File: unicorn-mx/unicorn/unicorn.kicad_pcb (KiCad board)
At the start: 2 copper layers, 267.6 x 110.5 mm, 118 parts, among them J2 USB_C, K1 KEYSW, K10 KEYSW, K11 KEYSW, K12 KEYSW, K13 KEYSW, K14 KEYSW, K15 KEYSW, K16 KEYSW, K17 KEYSW, K18 KEYSW, K19 KEYSW, K2 KEYSW, K20 KEYSW, K21 KEYSW, K22 KEYSW, K23 KEYSW, K24 KEYSW, K25 KEYSW, K26 KEYSW, K27 KEYSW, K28 KEYSW, K29 KEYSW, K3 KEYSW, K30 KEYSW, K31 KEYSW, K32 KEYSW, K33 KEYSW, K34 KEYSW, K35 KEYSW, K36 KEYSW, K37 KEYSW, K38 KEYSW, K39 KEYSW, K4 KEYSW, K40 KEYSW, K41 KEYSW, K42 KEYSW, K43 KEYSW, K44 KEYSW, K5 KEYSW, K6 KEYSW, K7 KEYSW, K8 KEYSW, K9 KEYSW, Q1 MMBT3904, SW1 SW_Push, SW2 Rotary_Encoder_Switch, SW3 Rotary_Encoder_Switch, U1 XC6206PxxxMR, U3 STM32F072CBUx, U4 SRV05-4

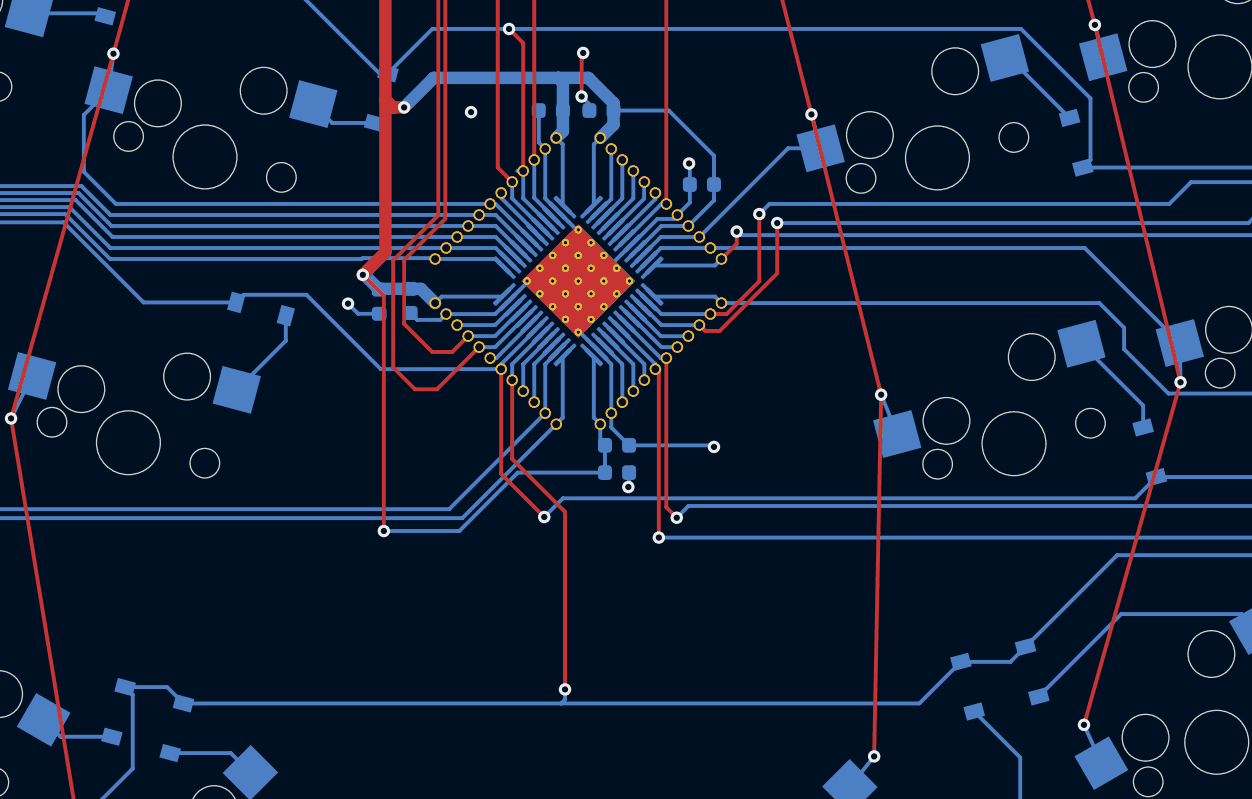
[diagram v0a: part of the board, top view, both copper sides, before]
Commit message: add 3d models, add oled
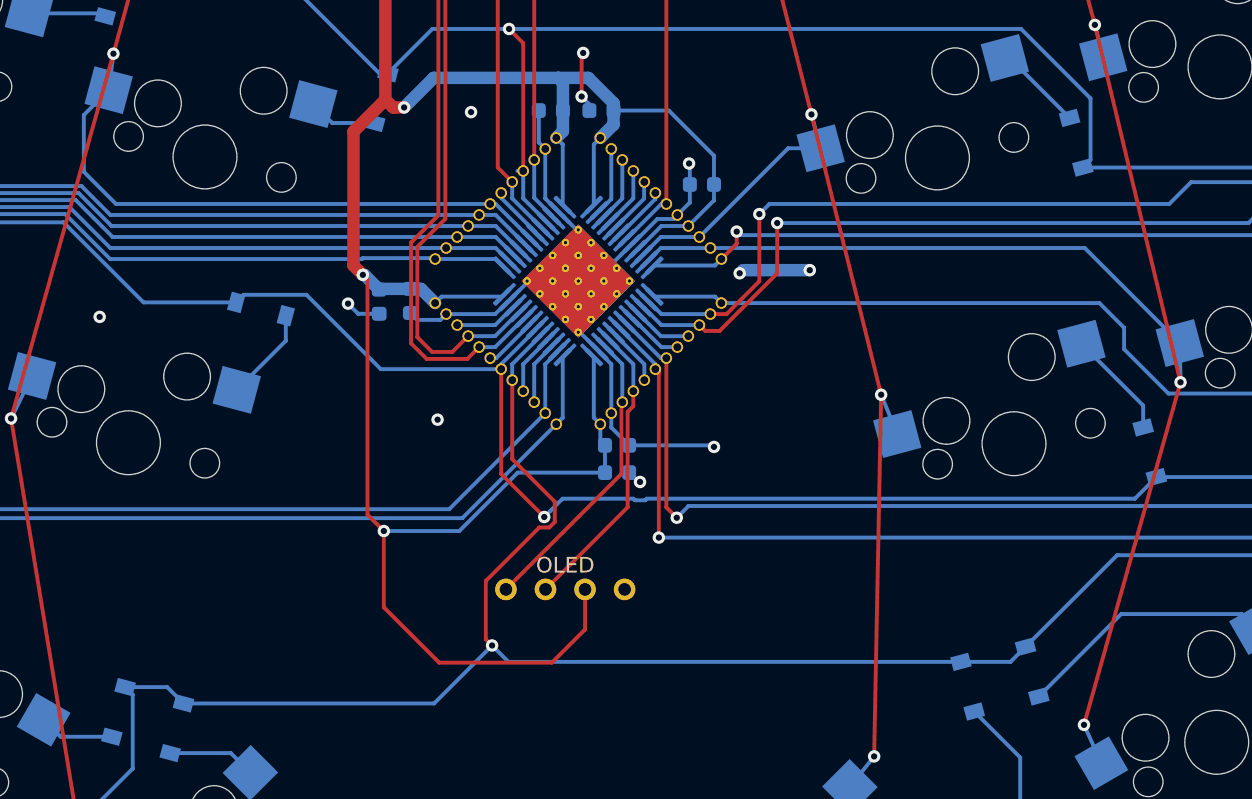
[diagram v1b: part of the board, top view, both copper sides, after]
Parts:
- added OL1: OLED, kbd:OLED_v2, F.Cu at (153.6, 100.6)
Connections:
- J2 pad A8: (no net) -> Net-(J2-PadA8)
- J2 pad B8: (no net) -> Net-(J2-PadB8)
- U4 pad 5: (no net) -> Net-(U4-Pad5)
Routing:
- net +3V3: track 161.1 -> 184.3 mm
- net i2c_sda: track 4.06 -> 19.2 mm
- net i2c_scl: track 3.86 -> 18.9 mm
- net GND: track 58.2 -> 62.8 mm, vias 10 -> 14
- net /D-: track 84.3 -> 80.2 mm
- net /row3: track 172.6 -> 171.7 mm
- net /D+: track 75.1 -> 74.4 mm

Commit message: finalize unicorn design
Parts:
- added H1: MountingHole, MountingHole:MountingHole_4.5mm, F.Cu at (260.1, 49.6)
- added H2: MountingHole, MountingHole:MountingHole_4.5mm, F.Cu at (269.0, 93.6)
- added H3: MountingHole, MountingHole:MountingHole_4.5mm, F.Cu at (47.6, 49.6)
- added H4: MountingHole, MountingHole:MountingHole_4.5mm, F.Cu at (184.1, 60.6)
- added H5: MountingHole, MountingHole:MountingHole_4.5mm, F.Cu at (39.0, 93.6)
- added H6: MountingHole, MountingHole:MountingHole_4.5mm, F.Cu at (123.6, 60.6)
- added H7: MountingHole, MountingHole:MountingHole_4.5mm, F.Cu at (154.0, 112.5)
- moved D46 25.6 mm to (148.3, 60.7)
- moved F1 25.6 mm to (155.2, 60.6)
- moved Q1 20.7 mm to (164.6, 65.0)
- moved R2 20.7 mm to (160.4, 63.0)
- moved C1 20.7 mm to (160.3, 66.4)
- moved C2 20.7 mm to (164.3, 69.6)
- moved D45 20.7 mm to (162.6, 59.6)
- moved R1 20.7 mm to (160.3, 64.8)
- moved R3 20.7 mm to (164.2, 67.8)
- moved R4 20.7 mm to (165.8, 58.9)
- moved R5 20.7 mm to (166.3, 62.0)
- moved C4 17.7 mm to (142.4, 62.0)
- moved U1 17.7 mm to (142.4, 59.3)
- moved U4 17.1 mm to (154.9, 66.3)
- moved SW1 15.5 mm to (153.7, 51.0)
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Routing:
- net +3V3: track 184.3 -> 163.4 mm, vias 4 -> 5
- net NRST: track 33.7 -> 14.4 mm
- net /D-: track 80.2 -> 61.7 mm, vias 2 -> 1
- net BOOT0: track 41.2 -> 25.7 mm
- net Net-(D25-Pad2): track 3.70 -> 16.4 mm
- net +5V: track 28.7 -> 17.4 mm
- net /D+: track 74.4 -> 64.9 mm
- net /row2: track 266.1 -> 256.9 mm
- net Net-(D2-Pad2): track 9.41 -> 13.8 mm
- net Net-(D1-Pad2): track 4.98 -> 9.06 mm
- net GND: track 62.8 -> 66.9 mm, vias 14 -> 8
- net Net-(J2-PadB5): track 6.51 -> 2.67 mm, vias 2 -> 0
- net Net-(D6-Pad2): track 5.46 -> 9.23 mm
- net /col1: track 162.4 -> 166.1 mm
- net /row1: track 265.1 -> 262.1 mm
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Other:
- board size 267.6 x 110.5 mm -> 268.2 x 110.5 mm
- board text added: "Unicorn Keyboard v1.0 Designed by Yang Hu"

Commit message: add plate and bottom, add rendered images
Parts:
- added BZ1: Buzzer, hy-keebs:Piezo-KLJ-1625, F.Cu at (154.0, 113.6)
- added D48: WS2812S, LED_SMD:LED_WS2812_PLCC6_5.0x5.0mm_P1.6mm, B.Cu at (119.0, 117.6)
- added D49: WS2812S, LED_SMD:LED_WS2812_PLCC6_5.0x5.0mm_P1.6mm, B.Cu at (54.0, 96.1)
- added D50: WS2812S, LED_SMD:LED_WS2812_PLCC6_5.0x5.0mm_P1.6mm, B.Cu at (38.5, 44.6)
- added D51: WS2812S, LED_SMD:LED_WS2812_PLCC6_5.0x5.0mm_P1.6mm, B.Cu at (114.0, 54.6)
- added D52: WS2812S, LED_SMD:LED_WS2812_PLCC6_5.0x5.0mm_P1.6mm, B.Cu at (194.0, 54.6)
- added D53: WS2812S, LED_SMD:LED_WS2812_PLCC6_5.0x5.0mm_P1.6mm, B.Cu at (269.5, 45.2)
- added D54: WS2812S, LED_SMD:LED_WS2812_PLCC6_5.0x5.0mm_P1.6mm, B.Cu at (255.0, 95.6)
- added D55: WS2812S, LED_SMD:LED_WS2812_PLCC6_5.0x5.0mm_P1.6mm, B.Cu at (189.0, 117.6)
- U3: footprint breakout_pins:Dual_MCU_QFP_QFN_48_with_breakout_pins -> Package_DFN_QFN:QFN-48-1EP_7x7mm_P0.5mm_EP5.15x5.15mm_ThermalVias
- moved H7 15.0 mm to (154.0, 127.6)
- moved D24 13.3 mm to (277.4, 59.5)
- moved D12 5.11 mm to (262.9, 41.9)
- moved D11 4.02 mm to (256.1, 40.0)
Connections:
- U3 pad 14: /col10 -> /buzzer_p
- U3 pad 15: /col11 -> /buzzer_n
- U3 pad 16: Net-(U3-Pad16) -> /col10
- U3 pad 17: Net-(U3-Pad17) -> /col11
- U3 pad 21: i2c_scl -> Net-(U3-Pad21)
- U3 pad 22: i2c_sda -> Net-(U3-Pad22)
- U3 pad 28: Net-(U3-Pad28) -> LED
- U3 pad 34: Net-(U3-Pad34) -> /col5
- U3 pad 42: /col5 -> i2c_scl
- U3 pad 43: Net-(U3-Pad43) -> i2c_sda
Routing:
- net +3V3: track 163.4 -> 625.0 mm, vias 5 -> 18
- net Net-(D51-Pad1): track 0.00 -> 104.2 mm, vias 0 -> 4
- net Net-(D52-Pad1): track 0.00 -> 80.1 mm
- net Net-(D50-Pad1): track 0.00 -> 79.9 mm
- net Net-(D54-Pad1): track 0.00 -> 75.1 mm, vias 0 -> 2
- net Net-(D48-Pad1): track 0.00 -> 74.6 mm, vias 0 -> 2
- net LED: track 0.00 -> 68.3 mm, vias 0 -> 2
- net Net-(D49-Pad1): track 0.00 -> 61.9 mm, vias 0 -> 2
- net Net-(D53-Pad1): track 0.00 -> 58.2 mm, vias 0 -> 2
- net /buzzer_n: track 0.00 -> 44.7 mm, vias 0 -> 1
- net /buzzer_p: track 0.00 -> 35.5 mm, vias 0 -> 1
- net i2c_sda: track 19.2 -> 35.2 mm, vias 0 -> 2
- net i2c_scl: track 18.9 -> 32.7 mm, vias 0 -> 2
- net Net-(D24-Pad2): track 4.82 -> 11.9 mm
- net /row1: track 262.1 -> 269.0 mm, vias 1 -> 2
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
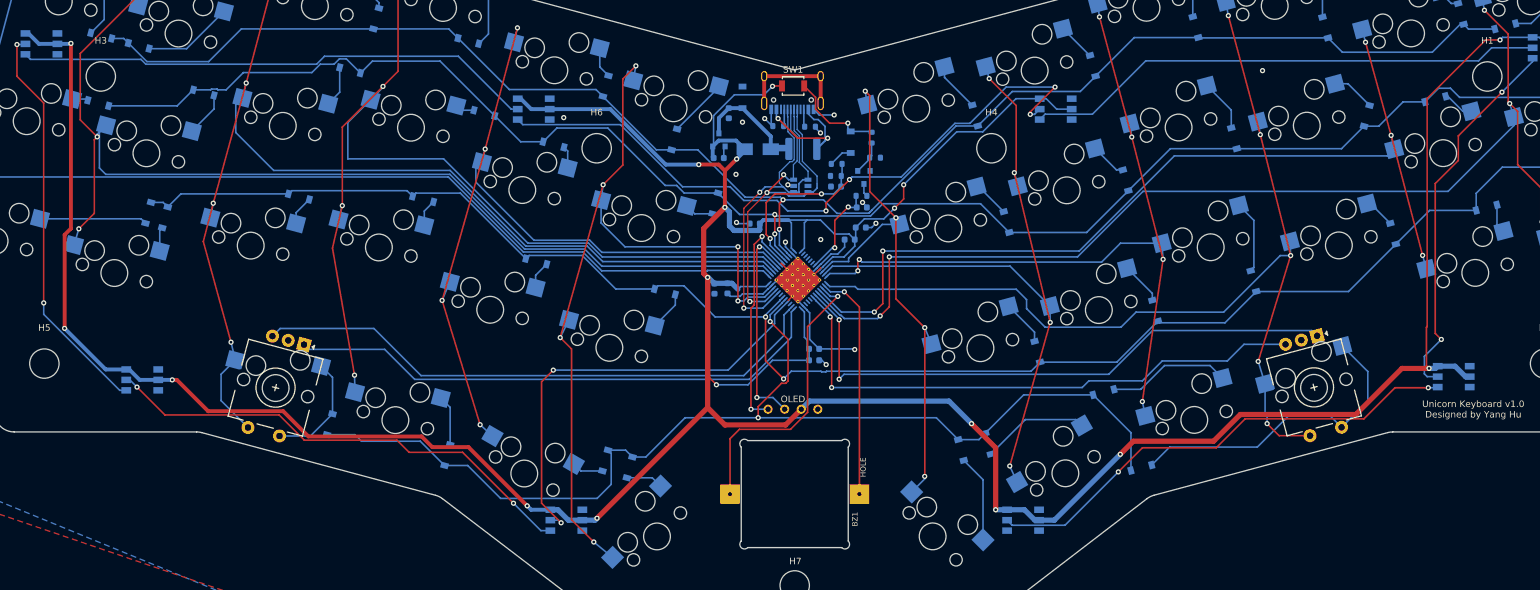
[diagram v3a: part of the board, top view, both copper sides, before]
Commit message: Add automation files: now use `make unicorn` or `make unicorn-doc` to generate output and `make clean` to clean up
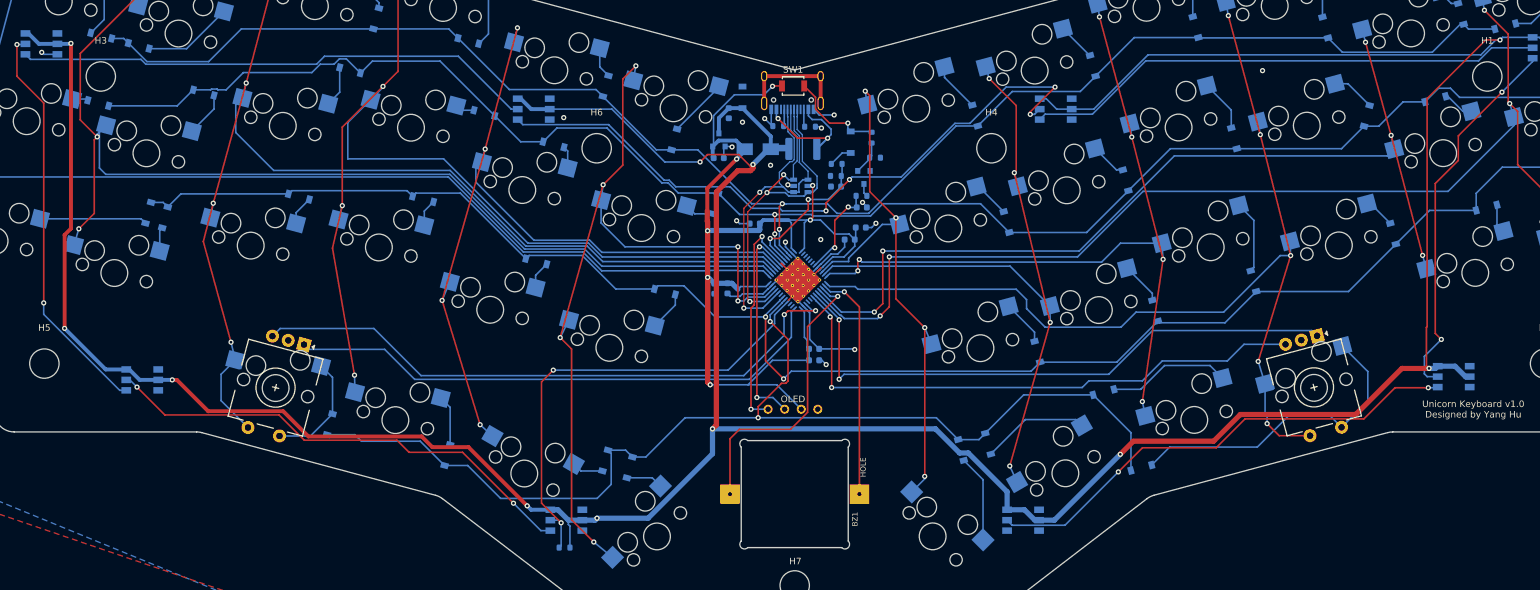
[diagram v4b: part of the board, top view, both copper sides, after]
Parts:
- added R6: 10k, Resistor_SMD:R_0603_1608Metric, B.Cu at (118.7, 121.8)
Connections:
- D48 pad 3: +3V3 -> +5V
- D48 pad 5: +3V3 -> +5V
- D49 pad 3: +3V3 -> +5V
- D49 pad 5: +3V3 -> +5V
- D50 pad 3: +3V3 -> +5V
- D50 pad 5: +3V3 -> +5V
- D51 pad 3: +3V3 -> +5V
- D51 pad 5: +3V3 -> +5V
- D52 pad 3: +3V3 -> +5V
- D52 pad 5: +3V3 -> +5V
- D53 pad 3: +3V3 -> +5V
- D53 pad 5: +3V3 -> +5V
- D54 pad 3: +3V3 -> +5V
- D54 pad 5: +3V3 -> +5V
- D55 pad 3: +3V3 -> +5V
- D55 pad 5: +3V3 -> +5V
- U3 pad 22: Net-(U3-Pad22) -> /ENC1B
- U3 pad 26: /ENC1B -> Net-(U3-Pad26)
- U4 pad 5: Net-(U4-Pad5) -> +3V3
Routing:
- net +5V: track 17.4 -> 559.2 mm, vias 0 -> 11
- net +3V3: track 625.0 -> 177.2 mm, vias 18 -> 7
- net /ENC1B: track 89.4 -> 94.6 mm, vias 0 -> 2
- net LED: track 68.3 -> 72.2 mm
- net GND: track 64.3 -> 67.8 mm, vias 17 -> 19
- net BOOT0: track 26.3 -> 23.1 mm
- net /VCC: track 20.7 -> 21.9 mm
- net /row0: track 250.6 -> 249.9 mm

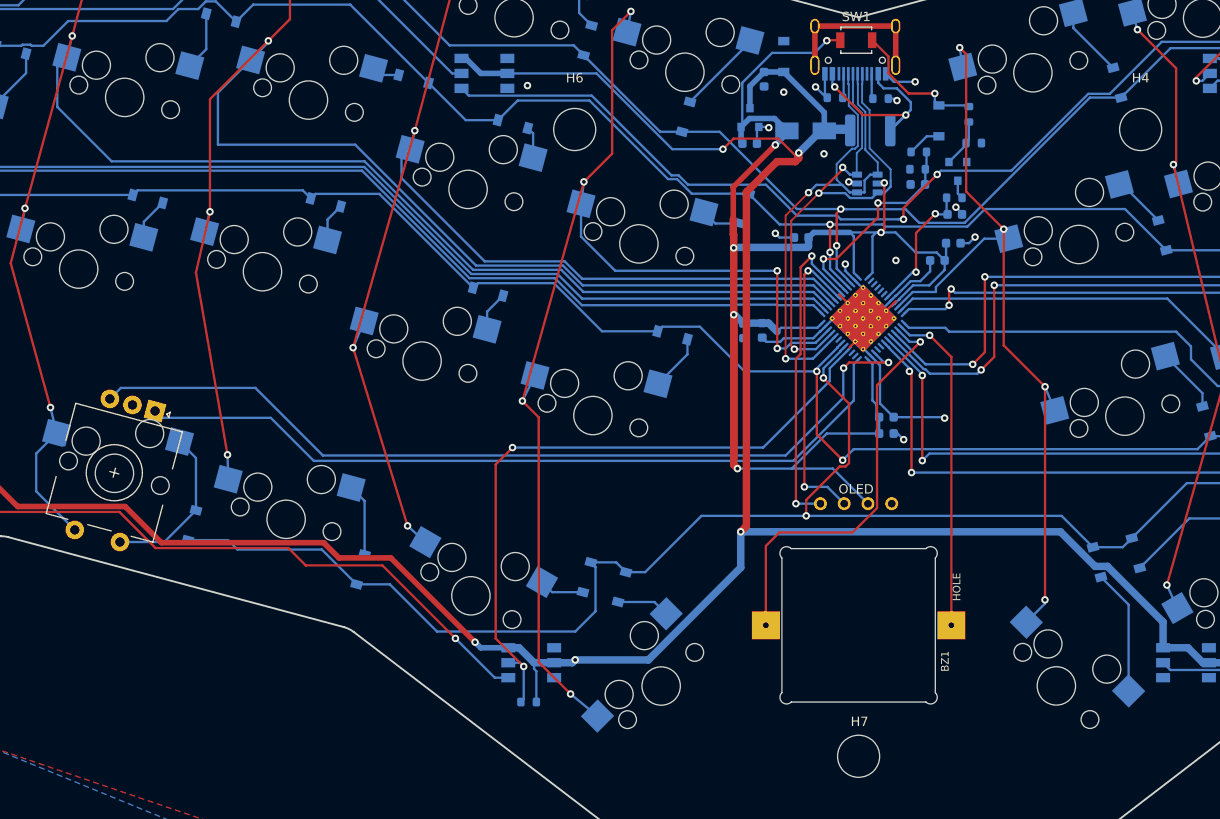
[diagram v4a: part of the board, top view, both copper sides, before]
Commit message: route pcb with new pin assginments, add bridges for led, add test points
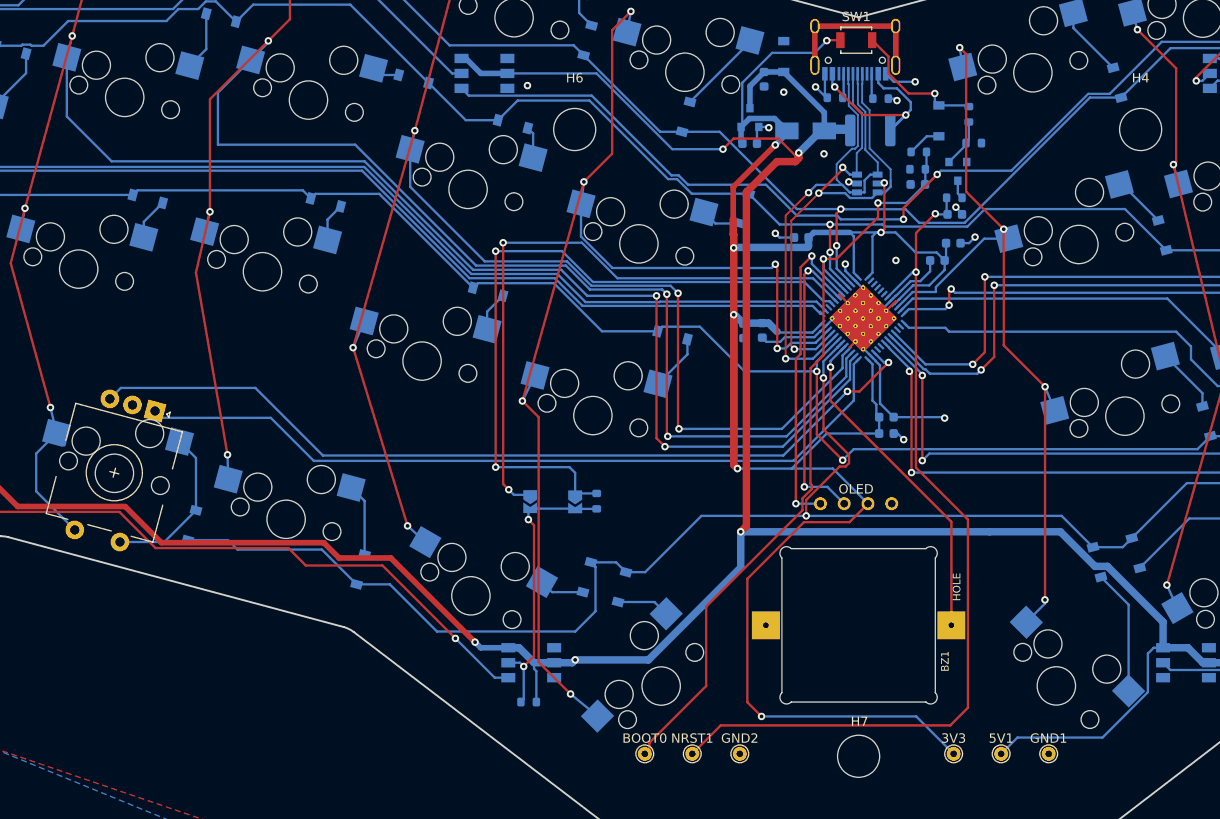
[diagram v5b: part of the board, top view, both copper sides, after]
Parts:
- added 3V3: TestPoint, TestPoint:TestPoint_THTPad_D1.5mm_Drill0.7mm, F.Cu at (164.2, 127.3)
- added 5V1: TestPoint, TestPoint:TestPoint_THTPad_D1.5mm_Drill0.7mm, F.Cu at (169.2, 127.3)
- added BOOT0: TestPoint, TestPoint:TestPoint_THTPad_D1.5mm_Drill0.7mm, F.Cu at (131.1, 127.3)
- added GND1: TestPoint, TestPoint:TestPoint_THTPad_D1.5mm_Drill0.7mm, F.Cu at (174.3, 127.3)
- added GND2: TestPoint, TestPoint:TestPoint_THTPad_D1.5mm_Drill0.7mm, F.Cu at (141.3, 127.3)
- added JP1: SolderJumper_2_Open, Jumper:SolderJumper-2_P1.3mm_Open_TrianglePad1.0x1.5mm, B.Cu at (118.9, 100.3)
- added JP2: SolderJumper_2_Open, Jumper:SolderJumper-2_P1.3mm_Open_TrianglePad1.0x1.5mm, B.Cu at (123.7, 100.4)
- added NRST1: TestPoint, TestPoint:TestPoint_THTPad_D1.5mm_Drill0.7mm, F.Cu at (136.2, 127.3)
- added R9: 0, Resistor_SMD:R_0603_1608Metric, B.Cu at (126.0, 100.3)
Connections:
- BZ1 pad 2: /buzzer_n -> GND
- U3 pad 14: /buzzer_p -> Net-(U3-Pad14)
- U3 pad 15: /buzzer_n -> Net-(U3-Pad15)
- U3 pad 26: Net-(U3-Pad26) -> /col2
- U3 pad 27: Net-(U3-Pad27) -> /col3
- U3 pad 28: LED -> /col4
- U3 pad 29: /row3 -> /buzzer_p
- U3 pad 30: /row2 -> /row3
- U3 pad 31: Net-(U3-Pad31) -> /row2
- U3 pad 39: /col2 -> Net-(U3-Pad39)
- U3 pad 40: /col3 -> LED_PWM
- U3 pad 41: /col4 -> LED_SPI
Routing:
- net NRST: track 14.4 -> 94.8 mm
- net LED_PWM: track 0.00 -> 74.9 mm, vias 0 -> 2
- net LED_SPI: track 0.00 -> 67.3 mm, vias 0 -> 2
- net BOOT0: track 23.1 -> 84.1 mm
- net +3V3: track 177.2 -> 231.0 mm, vias 7 -> 8
- net /buzzer_n: track 44.7 -> 0.00 mm, vias 1 -> 0
- net LED: track 72.2 -> 30.5 mm
- net +5V: track 559.2 -> 583.6 mm
- net /col2: track 175.3 -> 197.5 mm, vias 4 -> 6
- net /col3: track 155.5 -> 177.2 mm, vias 4 -> 6
- net /col4: track 128.5 -> 147.6 mm, vias 4 -> 6
- net /ENC1B: track 94.6 -> 92.8 mm
- net /buzzer_p: track 35.5 -> 36.6 mm
- net /row3: track 172.0 -> 173.0 mm
- net /col5: track 130.1 -> 130.7 mm
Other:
- board text added: "PWM"
- board text added: "SPI"
